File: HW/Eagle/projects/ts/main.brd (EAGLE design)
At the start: 100 x 80 mm, 0 parts

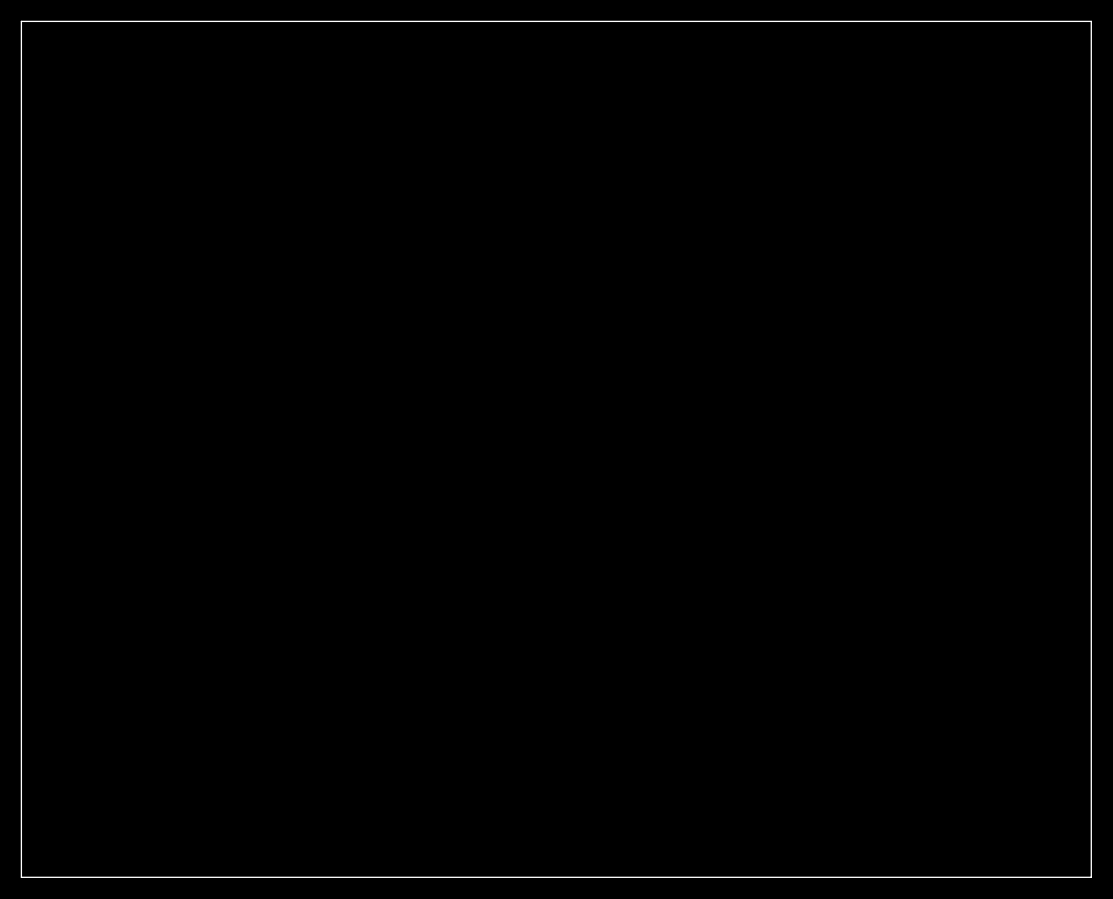
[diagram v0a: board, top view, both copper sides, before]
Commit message: Designed power supply
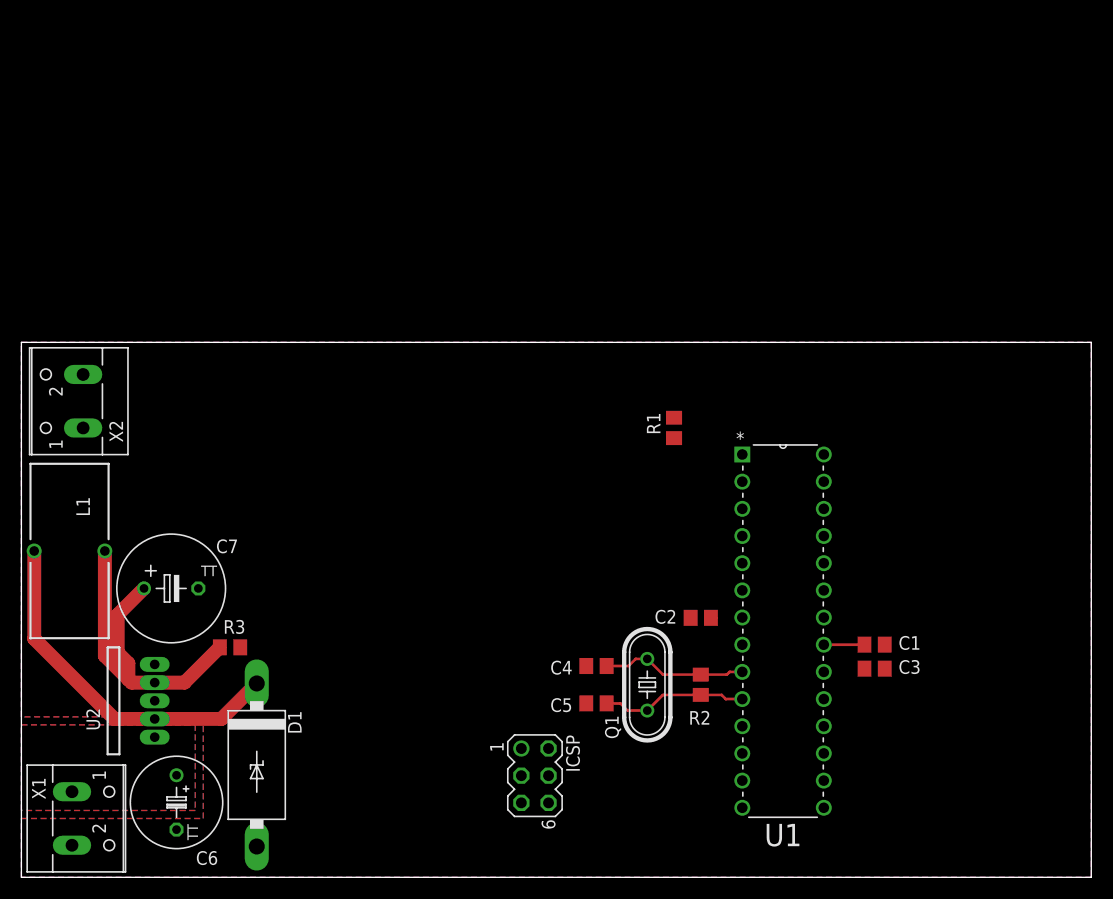
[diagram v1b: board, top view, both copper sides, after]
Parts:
- added C1, C2, C3: 100nF, rcl:C0805
- added C4, C5: 15pF, rcl:C0805
- added C6: 100uF, rcl:TAP5-80
- added C7: 1000uF, rcl:TT5D10
- added D1: 1N582X, misc:DIODE5MM
- added ICSP: (no value), con-lstb:MA03-2
- added L1: 100uH, rcl:TJ3-U1
- added Q1: (no value), crystal:HC49/S
- added R1: 10k, rcl:R0805
- added R2: 1M, rcl:R0805
- added R3: 0, rcl:R0805
- added U1: ATMEGA328P-PU, ATMEGA328P-PU:DIP254P762X457-28
- added U2: LM2576T, misc:TO220-5
- added X1, X2: (no value), con-wago-500:W237-102
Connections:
- new net +12V: C6.+, U2.1, X1.1
- new net GND: C1.2, C2.1, C3.1, C4.1, C5.1, C6.-, C7.-, D1.A, ICSP.6, U1.22, U1.8, U2.3, U2.5, X1.2
- new net N$1: C1.1, U1.21
- new net N$2: ICSP.1, U1.18
- new net N$3: C5.2, Q1.1, R2.1, U1.10
- new net N$4: C4.2, Q1.2, R2.2, U1.9
- new net N$5: ICSP.3, U1.19
- new net N$6: ICSP.4, U1.17
- new net N$7: D1.C, L1.2, U2.2
- new net N$8: C7.+, L1.1, R3.1, U2.4
- new net NRST: ICSP.5, R1.1, U1.1
- new net VCC: C2.2, C3.2, ICSP.2, R3.2, U1.20, U1.7
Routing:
- net N$7: track 0.00 -> 33.5 mm
- net N$8: track 0.00 -> 32.9 mm
- net N$3: track 0.00 -> 13.7 mm
- net N$4: track 0.00 -> 13.7 mm
- net N$1: track 0.00 -> 3.80 mm
- net VCC: track 0.00 -> 0.53 mm
- added copper zone on layer 1, net +12V
- added copper zone on layer 16, net +12V
- added copper zone on layer 1, net GND
- added copper zone on layer 16, net GND
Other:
- board size 100 x 80 mm -> 100 x 50 mm

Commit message: 3.3v supply
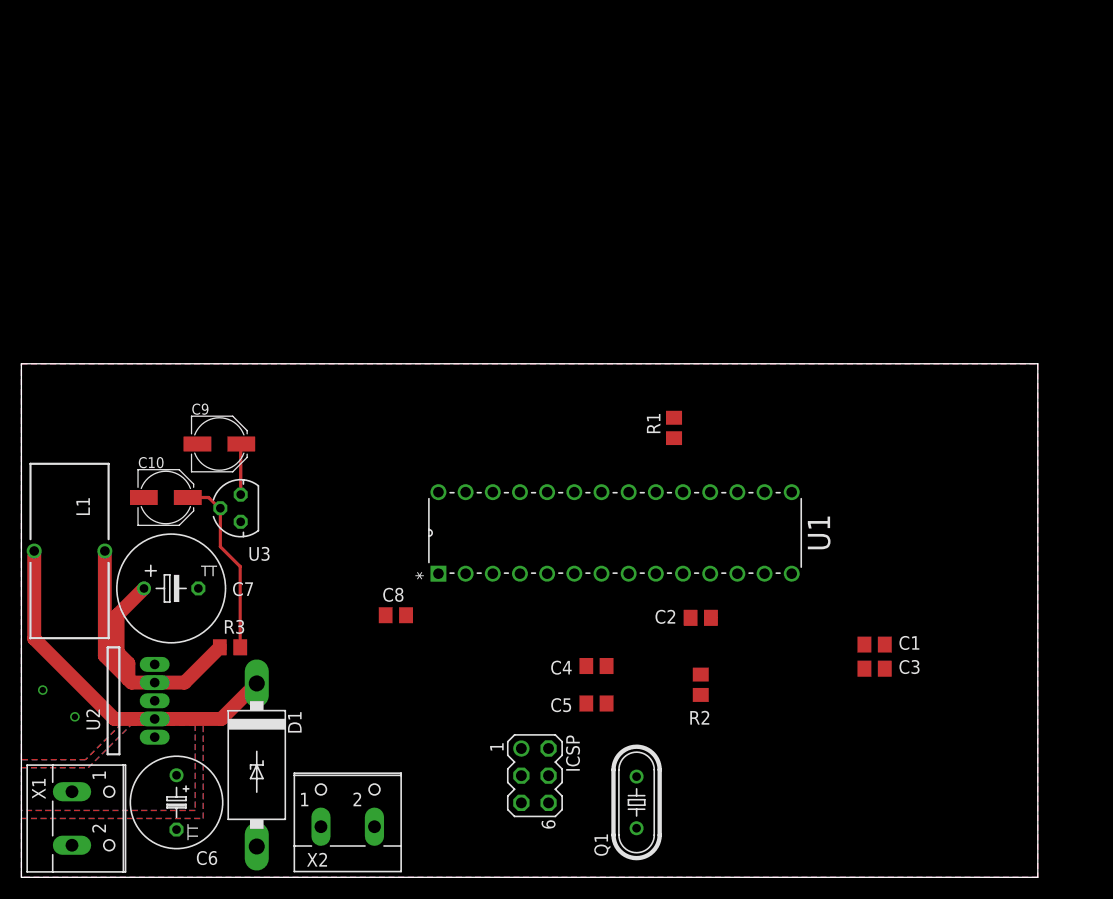
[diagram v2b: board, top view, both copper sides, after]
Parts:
- added C10, C9: 10uF, rcl:PANASONIC_C
- added C8: 100nF, rcl:C0805
- added U3: LE33CZ, v-reg:TO-92
- moved X2 46.5 mm to (30.5, 6.00), turned to 0 degrees
- moved U1 29.7 mm to (72.0, 36.0), turned to 90 degrees
- moved Q1 11.0 mm to (57.5, 7.00)
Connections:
- new net +3V3: C9.+, U3.3
- net GND: now also C10.-, C8.1, C9.-, U3.1
- net NRST: now also C8.2
- net VCC: now also C10.+, R1.2, U3.2
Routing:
- net VCC: track 0.53 -> 17.8 mm
- net N$3: track 13.7 -> 0.00 mm
- net N$4: track 13.7 -> 0.00 mm
- net +3V3: track 0.00 -> 4.75 mm
- net N$1: track 3.80 -> 0.00 mm
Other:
- board size 100 x 50 mm -> 95 x 48 mm

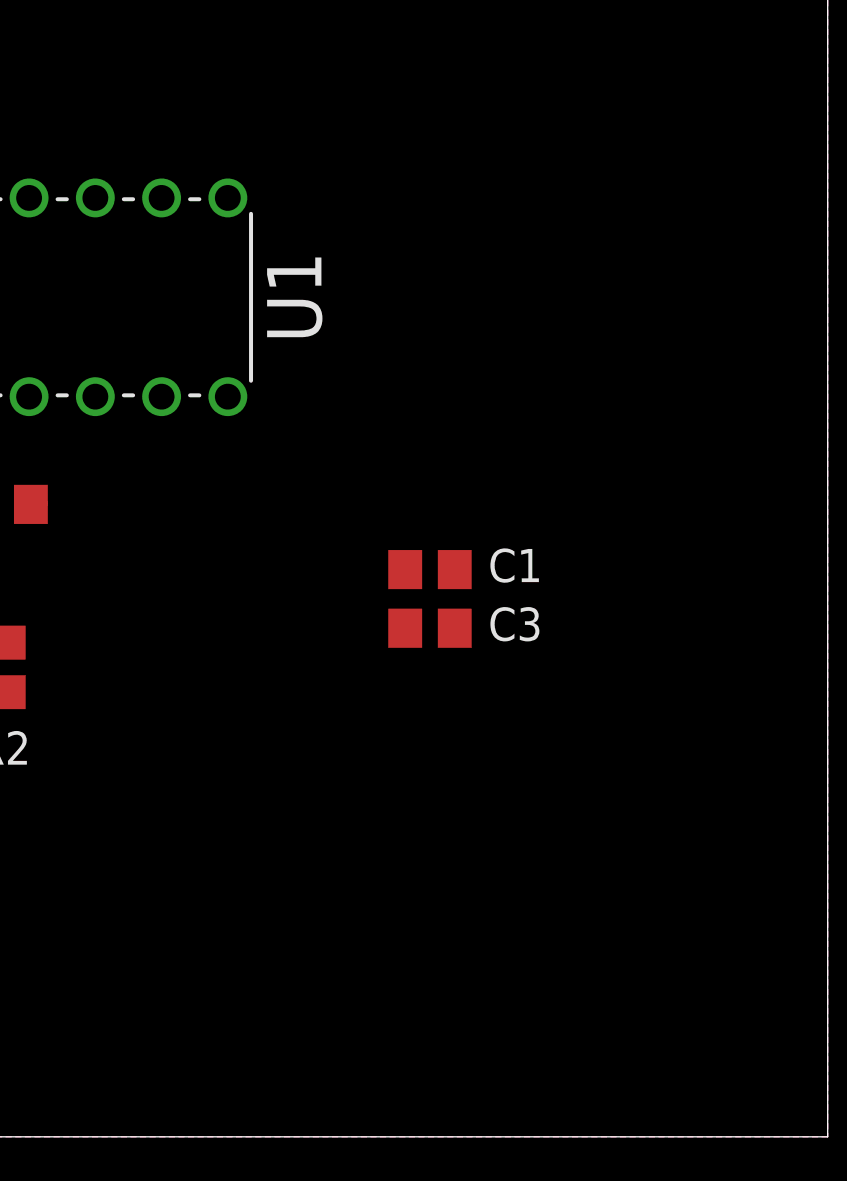
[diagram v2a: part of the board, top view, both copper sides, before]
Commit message: Added level shifter CMOS 4050
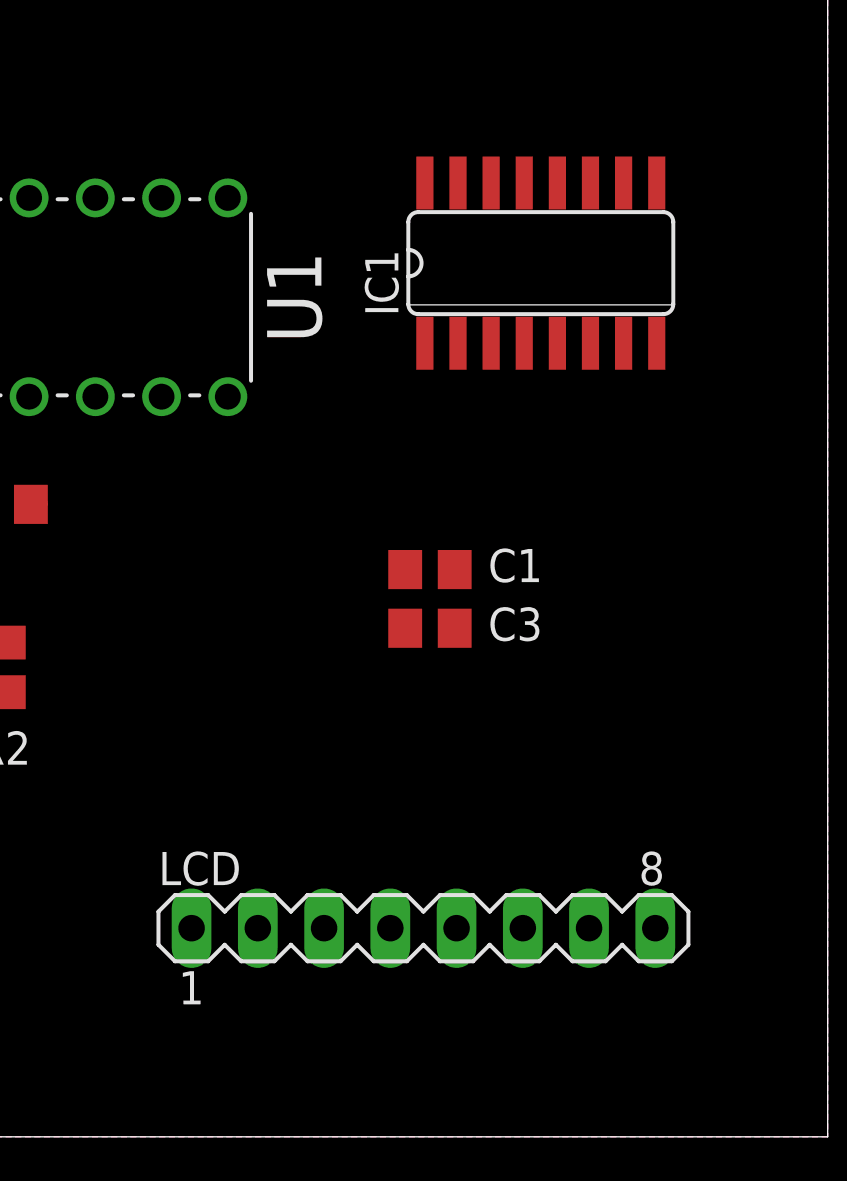
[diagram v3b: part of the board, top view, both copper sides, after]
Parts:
- added IC1: 4050D, 40xx:SO16
- added LCD: (no value), con-lstb:MA08-1
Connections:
- net +3V3: now also IC1.1, LCD.1
- net GND: now also IC1.8, LCD.2
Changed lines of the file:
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@@
 <element name="C9" library="rcl" package="PANASONIC_C" value="10uF" x="18.5" y="40.5"/>
 <element name="C10" library="rcl" package="PANASONIC_C" value="10uF" x="13.5" y="35.5"/>
+<element name="IC1" library="40xx" package="SO16" value="4050D" x="84" y="33.5"/>
+<element name="LCD" library="con-lstb" package="MA08-1" value="" x="79.5" y="8">
+<attribute name="OC_NEWARK" value="unknown" x="79.5" y="8" size="1.778" layer="27" display="off"/>
+<attribute name="MPN" value="" x="79.5" y="8" size="1.778" layer="27" display="off"/>
+<attribute name="MF" value="" x="79.5" y="8" size="1.778" layer="27" display="off"/>
+<attribute name="OC_FARNELL" value="unknown" x="79.5" y="8" size="1.778" layer="27" display="off"/>
+</element>
 </elements>
 <signals>
@@
 <contactref element="C10" pad="-"/>
 <contactref element="C9" pad="-"/>
+<contactref element="IC1" pad="8"/>
+<contactref element="LCD" pad="2"/>
 </signal>
 <signal name="VCC">
@@
 <wire x1="20.5" y1="35.77" x2="20.5" y2="40.45" width="0.3" layer="1"/>
 <wire x1="20.5" y1="40.45" x2="20.55" y2="40.5" width="0.3" layer="1"/>
+<contactref element="IC1" pad="1"/>
+<contactref element="LCD" pad="1"/>
+<wire x1="70.61" y1="8" x2="79.555" y2="30.4266" width="0" layer="19" extent="1-1"/>
+<wire x1="20.5" y1="35.77" x2="70.61" y2="8" width="0" layer="19" extent="1-1"/>
 </signal>
 </signals>

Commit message: Many changes
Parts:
- added C11: 100nF, rcl:C0805
- added L2: 10uH, misc:L1206
- added R4: 330R, rcl:R0805
- added R5: 0R, rcl:R0805
- added RESET: (no value), switch-omron:B3F-10XX
- R3: value 0 -> 0R
- U3: value LE33CZ -> HT7533
- moved LCD 55.2 mm to (34.5, 40.0)
- moved IC1 46.0 mm to (38.0, 33.0)
- moved U1 30.7 mm to (68.5, 5.50), turned to 0 degrees
- moved C8 29.1 mm to (59.0, 41.0)
- moved C3 22.4 mm to (57.5, 21.8), turned to 90 degrees
- moved C9 13.6 mm to (5.00, 39.0)
- moved C2 11.4 mm to (73.2, 18.2), turned to 180 degrees
- moved L1 11.0 mm to (4.50, 19.5)
- moved Q1 10.8 mm to (53.5, 17.0)
- moved U3 9.71 mm to (11.0, 36.5), turned to 180 degrees
- moved C10 8.86 mm to (5.00, 33.0)
- moved ICSP 7.28 mm to (41.0, 7.50), turned to 180 degrees
- moved C1 6.62 mm to (73.2, 20.5)
- moved R2 6.08 mm to (57.5, 17.0)
- moved C5 6.01 mm to (53.5, 10.2)
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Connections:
- net N$1 renamed AREF
- net N$2 renamed MISO
- removed net N$5: ICSP.3, U1.19
- removed net N$6: ICSP.4, U1.17
- new net AVCC: C2.2, L2.1, U1.20
- new net LCD_DC: IC1.15, LCD.5
- new net LCD_LED: LCD.8, R4.2
- new net LCD_MOSI: IC1.12, LCD.6
- new net LCD_RST: IC1.4, LCD.4
- new net LCD_SCE: IC1.2, LCD.3
- new net LCD_SCK: IC1.10, LCD.7
- new net MOSI: IC1.11, ICSP.4, U1.17
- new net N$1: C9.+, R5.2, U3.3
- new net N$2: R4.1
- new net RXD: U1.2
- new net SCK: IC1.9, ICSP.3, U1.19
- new net TXD: U1.3
- net +3V3: now also C11.2, R5.1; no longer C9.+, U3.3
- net GND: now also C11.1, IC1.7, RESET.3
- net NRST: now also RESET.1
- net VCC: now also L2.2; no longer C2.2, U1.20
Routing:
- net VCC: track 17.8 -> 176.4 mm, vias 0 -> 2
- net NRST: track 0.00 -> 106.3 mm, vias 0 -> 1
- net SCK: track 0.00 -> 41.3 mm
- net MOSI: track 0.00 -> 37.1 mm
- net MISO: track 0.00 -> 36.0 mm
- net N$8: track 32.9 -> 0.00 mm
- net AVCC: track 0.00 -> 21.1 mm
- net LCD_RST: track 0.00 -> 13.4 mm
- net LCD_SCE: track 0.00 -> 11.8 mm
- net +3V3: track 4.75 -> 16.4 mm
- net N$7: track 33.5 -> 24.1 mm
- net N$3: track 0.00 -> 8.15 mm
- net N$4: track 0.00 -> 8.09 mm
- net N$1: track 0.00 -> 7.34 mm
- net LCD_DC: track 0.00 -> 4.32 mm
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- added copper zone on layer 1, net N$8
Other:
- board size 95 x 48 mm -> 85 x 45 mm
